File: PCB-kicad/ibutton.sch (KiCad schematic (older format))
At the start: 29 parts, among them J1 I_BUTTON, J2 IB_READ, J3 BATTERY, J4 USB_OTG, Q1 BC847, Q2 BC847, SW1 SW_Push, U1 ATMEGA8-16AU, U2 CH340G, Y1 12MHz

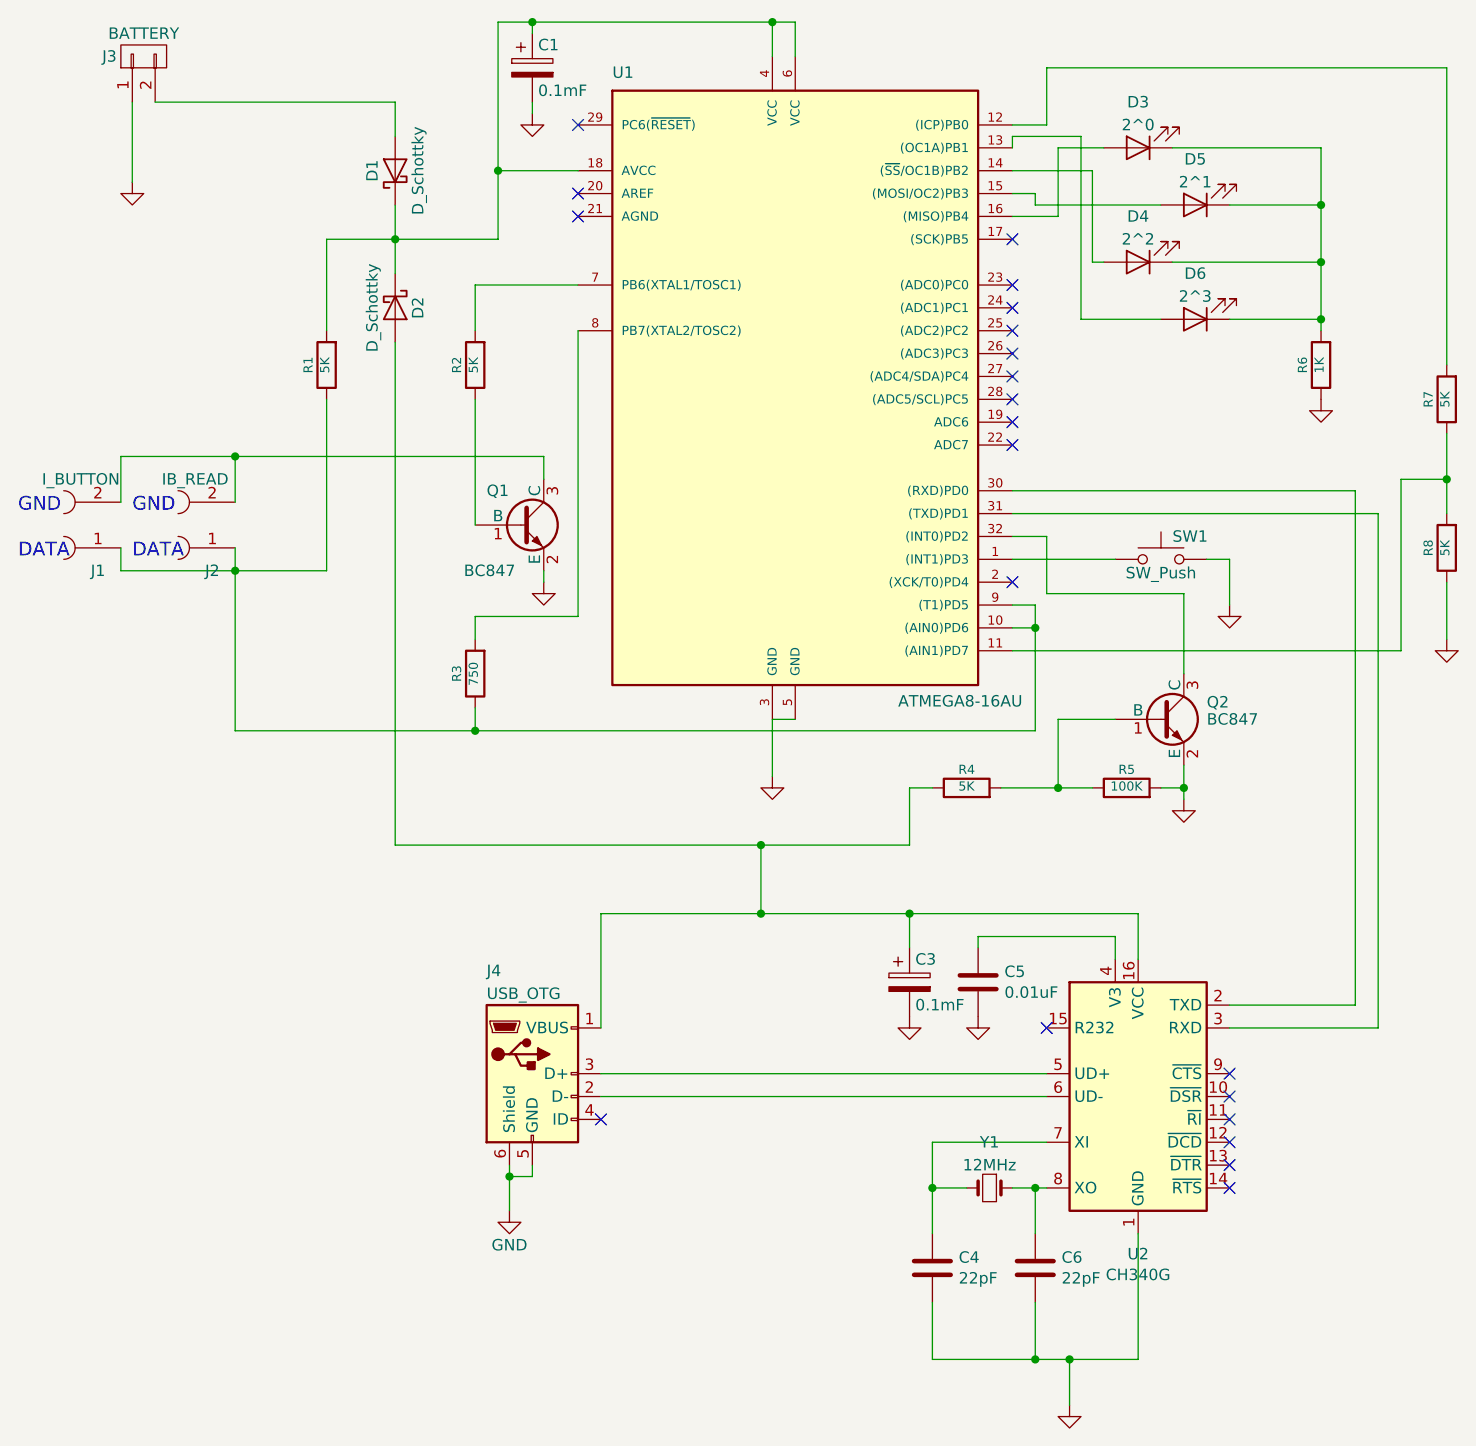
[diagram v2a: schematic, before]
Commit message: invalid footprint
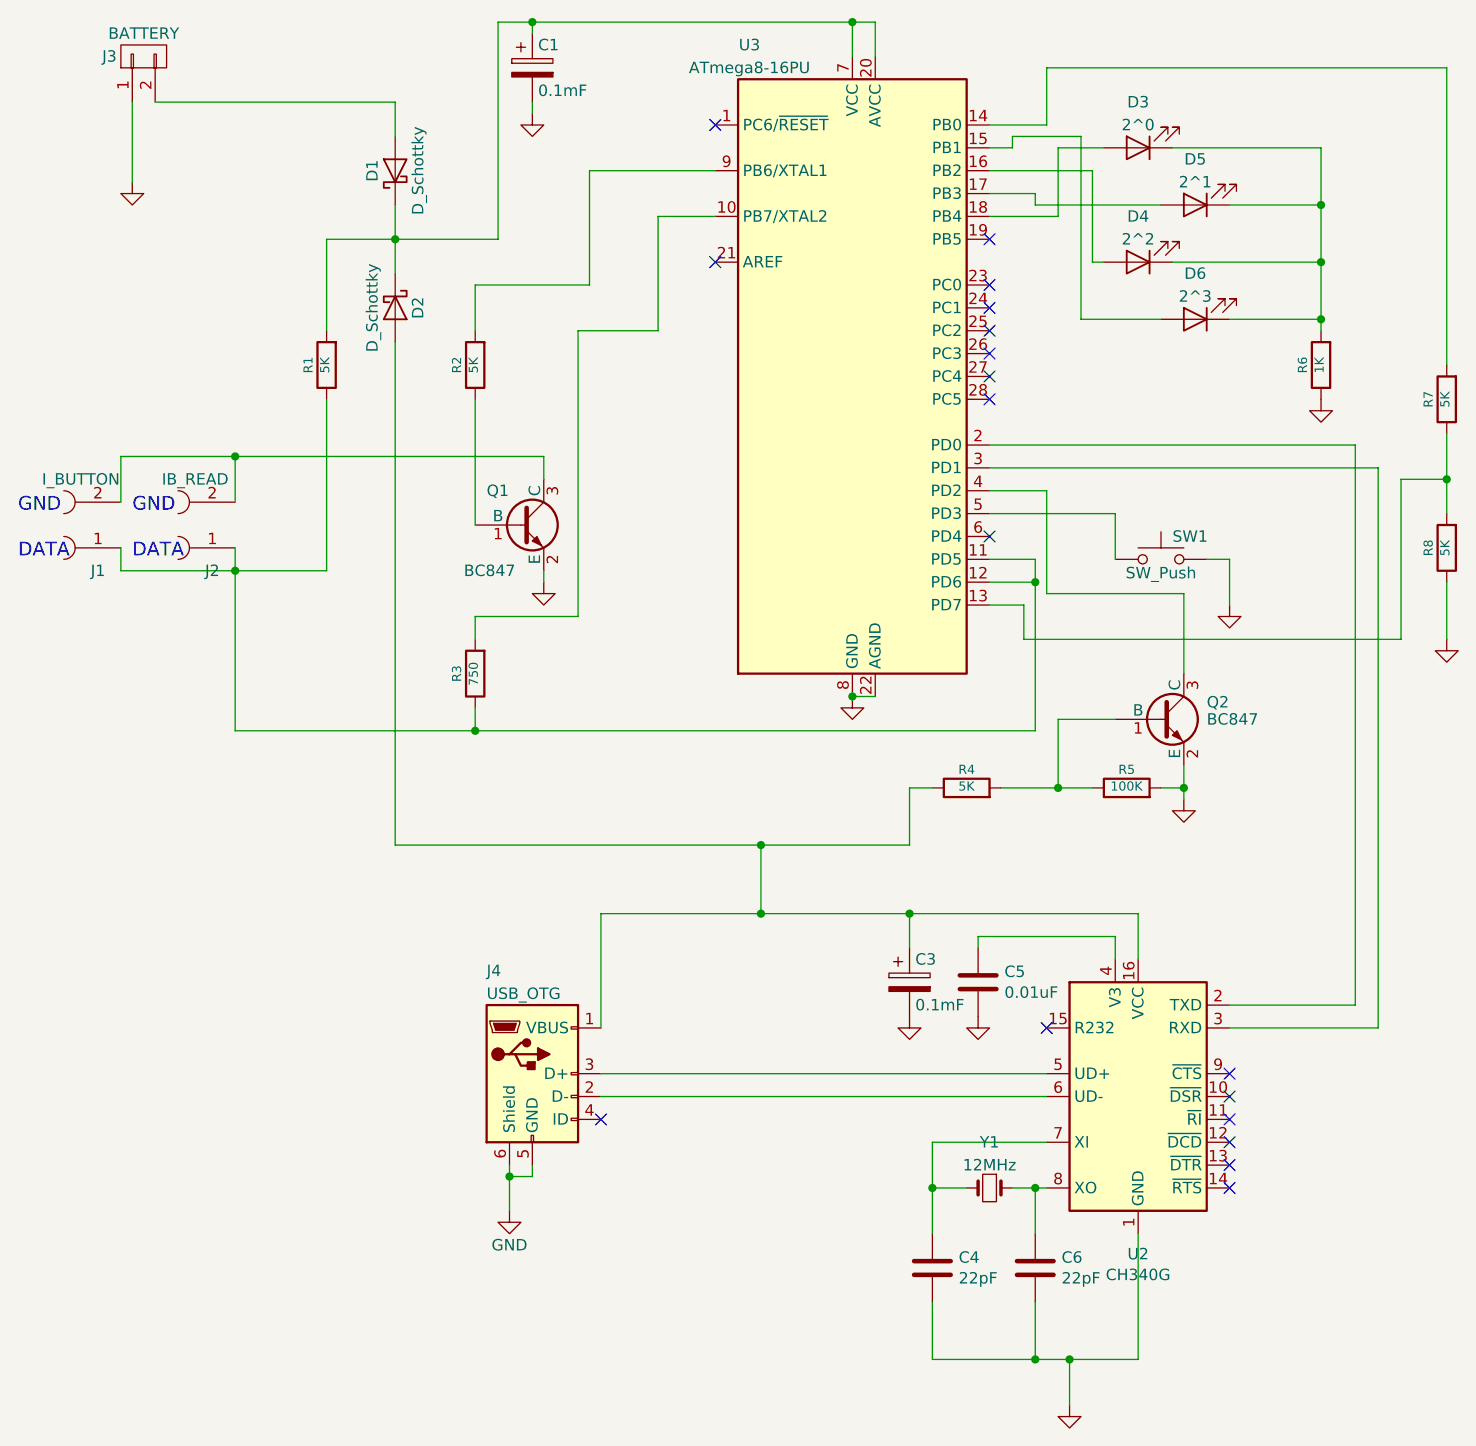
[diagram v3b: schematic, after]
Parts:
- removed U1: ATMEGA8-16AU, Package_DIP:DIP-32_W7.62mm, symbol ibutton-rescue:ATMEGA8-16AU
- added U3: ATmega8-16PU, Package_DIP:DIP-28_W7.62mm, symbol MCU_Microchip_ATmega:ATmega8-16PU
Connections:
- net GND: now also U3.22 (AGND), U3.8 (GND)
- net at R7.1, R8.2: now also U3.13 (PD7)
- net at R7.2: now also U3.14 (PB0)
- net at R2.2: now also U3.9 (PB6/XTAL1)
- net at J1.1, J2.1, R1.1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: now also U3.11 (PD5), U3.12 (PD6)
- net at C1.1, D1.1 (K), D2.1 (K)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: now also U3.20 (AVCC), U3.7 (VCC)
- net at R3.2: now also U3.10 (PB7/XTAL2)
- net at SW1.1: now also U3.5 (PD3)
- net at D6.2 (A): now also U3.15 (PB1)
- net at D4.2 (A): now also U3.16 (PB2)
- net at D5.2 (A): now also U3.17 (PB3)
- net at D3.2 (A): now also U3.18 (PB4)
- net at U2.2 (TXD): now also U3.2 (PD0)
- net at U2.3 (RXD): now also U3.3 (PD1)
- net at Q2.3 (C): now also U3.4 (PD2)
- no-connect marks 21 -> 18
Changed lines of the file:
@@
 L power:GND #PWR04
 U 1 1 52DFEEB0
-P 4900 4100
-F 0 "#PWR04" H 4900 4100 30  0001 C CNN
-F 1 "GND" H 4900 4030 30  0001 C CNN
-F 2 "" H 4900 4100 60  0000 C CNN
-F 3 "" H 4900 4100 60  0000 C CNN
-	1    4900 4100
+P 5250 3750
+F 0 "#PWR04" H 5250 3750 30  0001 C CNN
+F 1 "GND" H 5250 3680 30  0001 C CNN
+F 2 "" H 5250 3750 60  0000 C CNN
+F 3 "" H 5250 3750 60  0000 C CNN
+	1    5250 3750
 	1    0    0    -1
 $EndComp
@@
 Connection ~ 6200 6650
 Wire Wire Line
-	5950 2850 7450 2850
-Wire Wire Line
-	5950 2950 7550 2950
-Wire Wire Line
-	5950 3150 6400 3150
-Wire Wire Line
 	3250 2200 3250 4400
 Wire Wire Line
-	5000 3850 4900 3850
-Wire Wire Line
-	4900 3850 4900 4100
-Wire Wire Line
 	3250 1600 3250 1750
 Wire Wire Line
 	2950 1750 3250 1750
 Wire Wire Line
-	3700 1750 3700 1450
-Wire Wire Line
 	3700 800  3850 800
-Wire Wire Line
-	4900 800  4900 950
 Connection ~ 3250 1750
 Wire Wire Line
@@
 	6700 3300 6100 3300
 Wire Wire Line
-	6100 3300 6100 3050
-Wire Wire Line
-	6100 3050 5950 3050
-Wire Wire Line
 	5900 4150 6150 4150
 Wire Wire Line
@@
 Wire Wire Line
 	7850 3250 7850 3500
-Wire Wire Line
-	5950 3550 7650 3550
-Wire Wire Line
-	7650 3550 7650 2800
-Wire Wire Line
-	7650 2800 7850 2800
 Connection ~ 7850 2800
 Wire Wire Line
 	5500 4400 5500 4150
 Wire Wire Line
-	4050 1950 3600 1950
-Wire Wire Line
 	3600 1950 3600 2150
 Wire Wire Line
 	3600 2450 3600 3000
-Wire Wire Line
-	2550 3900 3600 3900
-Wire Wire Line
-	6050 3900 6050 3450
-Wire Wire Line
-	6050 3350 5950 3350
-Wire Wire Line
-	5950 3450 6050 3450
-Connection ~ 6050 3450
 $Comp
 L Device:R R6
@@
 Wire Wire Line
 	4050 3400 3600 3400
-Wire Wire Line
-	3700 1450 4050 1450
-Connection ~ 3700 1450
 $Comp
 L power:GND #PWR09
@@
 	6200 6650 6200 6850
 $Comp
-L ibutton-rescue:ATMEGA8-16AU U1
-U 1 1 59909598
-P 4950 2250
-F 0 "U1" H 4200 3450 50  0000 L BNN
-F 1 "ATMEGA8-16AU" H 5450 700 50  0000 L BNN
-F 2 "Package_DIP:DIP-32_W7.62mm" H 4950 2250 50  0001 C CIN
-F 3 "" H 4950 2250 50  0001 C CNN
-	1    4950 2250
-	1    0    0    -1
-$EndComp
-$Comp
 L ibutton-rescue:SW_Push SW1
 U 1 1 59909D47
@@
 Wire Wire Line
 	5500 4150 5600 4150
-Wire Wire Line
-	5000 800  5000 950
-Connection ~ 4900 800
 Wire Wire Line
 	3850 850  3850 800
@@
 Wire Wire Line
 	3900 2800 3900 2700
-Wire Wire Line
-	3900 2700 2550 2700
 Wire Wire Line
 	2050 2700 2050 2900
@@
 	7850 2800 7850 2950
 Wire Wire Line
-	6050 3450 6050 3350
-Wire Wire Line
-	3700 1450 3700 800
-Wire Wire Line
 	3750 5850 3750 6000
-Wire Wire Line
-	4900 800  5000 800
-Wire Wire Line
-	3850 800  4900 800
-Wire Wire Line
-	2550 3200 2950 3200
 Wire Wire Line
 	2550 3200 2550 3900
@@
 $EndComp
 Wire Wire Line
-	7450 2850 7450 5100
-Wire Wire Line
-	7550 2950 7550 5200
-Wire Wire Line
 	6500 6100 6500 6650
 Wire Wire Line
@@
 	5500 4700 6500 4700
 Wire Wire Line
-	5950 1250 6100 1250
-Wire Wire Line
 	6100 1250 6100 1000
 $Comp
@@
 Wire Wire Line
 	6250 2100 6600 2100
-NoConn ~ 5950 3250
+NoConn ~ 5850 3050
 NoConn ~ 4150 5600
-NoConn ~ 4050 1550
-NoConn ~ 4050 1650
-NoConn ~ 4050 1250
-NoConn ~ 5950 2650
-NoConn ~ 5950 2550
-NoConn ~ 5950 2450
-NoConn ~ 5950 2350
-NoConn ~ 5950 2250
-NoConn ~ 5950 2150
-NoConn ~ 5950 2050
-NoConn ~ 5950 1950
-NoConn ~ 5950 1750
+NoConn ~ 4650 1250
+NoConn ~ 5850 2450
+NoConn ~ 5850 2350
+NoConn ~ 5850 2250
+NoConn ~ 5850 2150
+NoConn ~ 5850 2050
+NoConn ~ 5850 1950
+NoConn ~ 5850 1750
 Wire Wire Line
 	6350 1350 6150 1350
@@
 	6150 1350 6150 1650
 Wire Wire Line
-	6150 1650 5950 1650
-Wire Wire Line
 	6600 1600 6050 1600
 Wire Wire Line
 	6050 1600 6050 1550
-Wire Wire Line
-	6050 1550 5950 1550
-Wire Wire Line
-	6300 1450 5950 1450
 Wire Wire Line
 	6300 1450 6300 1850
@@
 Wire Wire Line
 	4850 4400 5500 4400
+$Comp
+L MCU_Microchip_ATmega:ATmega8-16PU U3
+U 1 1 5EB77FFF
+P 5250 2350
+F 0 "U3" H 4800 3800 50  0000 C CNN
+F 1 "ATmega8-16PU" H 4800 3700 50  0000 C CNN
+F 2 "Package_DIP:DIP-28_W7.62mm" H 5250 2350 50  0001 C CIN
+F 3 "http://ww1.microchip.com/downloads/en/DeviceDoc/atmel-2486-8-bit-avr-microcontroller-atmega8_l_datasheet.pdf" H 5250 2350 50  0001 C CNN
+	1    5250 2350
+	1    0    0    -1
+$EndComp
+Wire Wire Line
+	5850 1250 6100 1250
+Wire Wire Line
+	5850 1350 5950 1350
+Wire Wire Line
+	5850 1450 6300 1450
+Wire Wire Line
+	5850 1550 6050 1550
+Wire Wire Line
+	5850 1650 6150 1650
+Wire Wire Line
+	7450 2650 5850 2650
+Wire Wire Line
+	7450 2650 7450 5100
+Wire Wire Line
+	7550 2750 5850 2750
+Wire Wire Line
+	7550 2750 7550 5200
+Wire Wire Line
+	6100 2850 5850 2850
+Wire Wire Line
+	6100 2850 6100 3300
+Wire Wire Line
+	6400 3150 6400 2950
+Wire Wire Line
+	6400 2950 5850 2950
+Wire Wire Line
+	6050 3150 5850 3150
+Wire Wire Line
+	2550 3900 3600 3900
+Wire Wire Line
+	2550 2700 3900 2700
+Wire Wire Line
+	2550 3200 2950 3200
+Wire Wire Line
+	6050 3150 6050 3250
+Wire Wire Line
+	5850 3250 6050 3250
+Connection ~ 6050 3250
+Wire Wire Line
+	6050 3250 6050 3900
+Wire Wire Line
+	7650 2800 7850 2800
+Wire Wire Line
+	5850 3350 6000 3350
+Wire Wire Line
+	6000 3350 6000 3500
+Wire Wire Line
+	6000 3500 7650 3500
+Wire Wire Line
+	7650 3500 7650 2800
+Wire Wire Line
+	5350 3750 5250 3750
+Connection ~ 5250 3750
+Wire Wire Line
+	4100 1950 4100 1450
+Wire Wire Line
+	4100 1450 4650 1450
+Wire Wire Line
+	3600 1950 4100 1950
+Wire Wire Line
+	4050 2150 4400 2150
+Wire Wire Line
+	4400 2150 4400 1650
+Wire Wire Line
+	4400 1650 4650 1650
+Wire Wire Line
+	3700 800  3700 1750
+Wire Wire Line
+	5250 800  5250 950
+Wire Wire Line
+	3850 800  5250 800
+Wire Wire Line
+	5250 800  5350 800
+Wire Wire Line
+	5350 800  5350 950
+Connection ~ 5250 800
+NoConn ~ 4650 1850
 $EndSCHEMATC
